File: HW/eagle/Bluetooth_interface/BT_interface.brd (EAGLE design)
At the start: 40 x 30 mm, 30 parts, among them IC3 FT232RL, IC5 UA78M05DCY

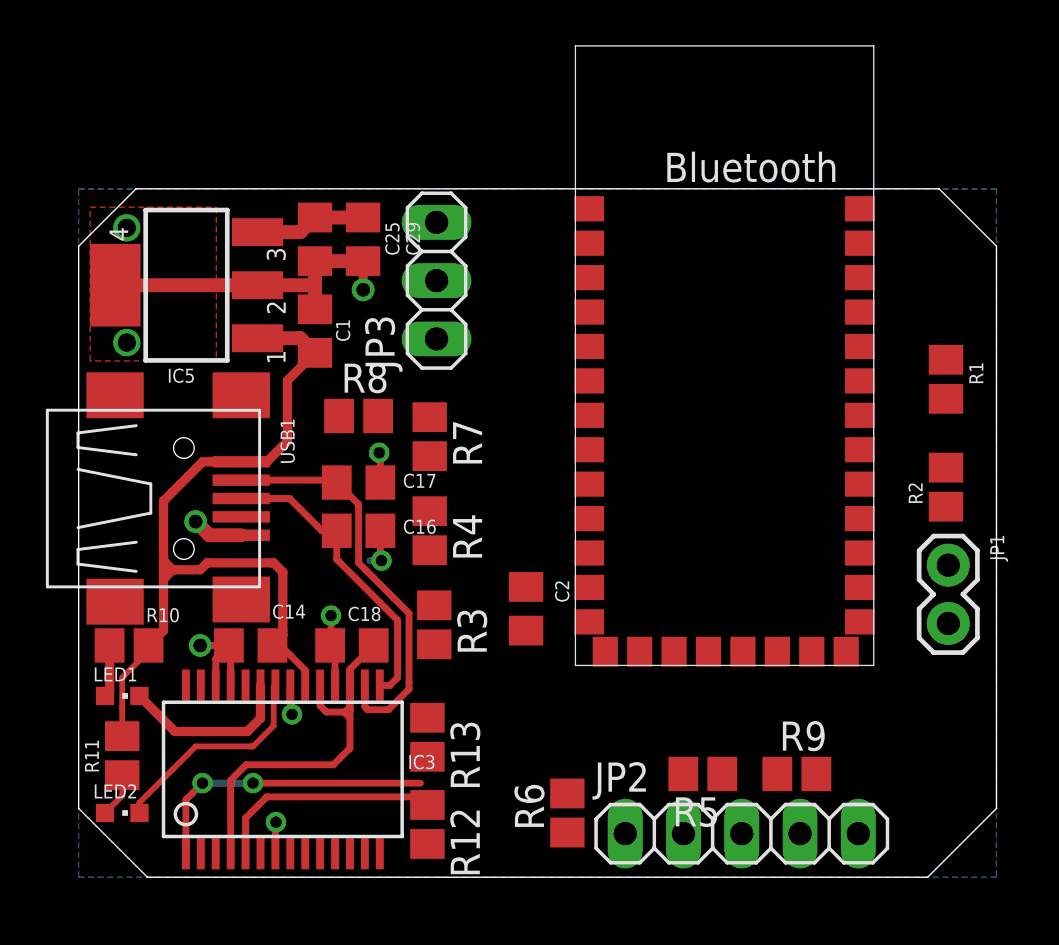
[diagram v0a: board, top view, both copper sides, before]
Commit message: labels changed, parts smashed, labels resized and rearranged
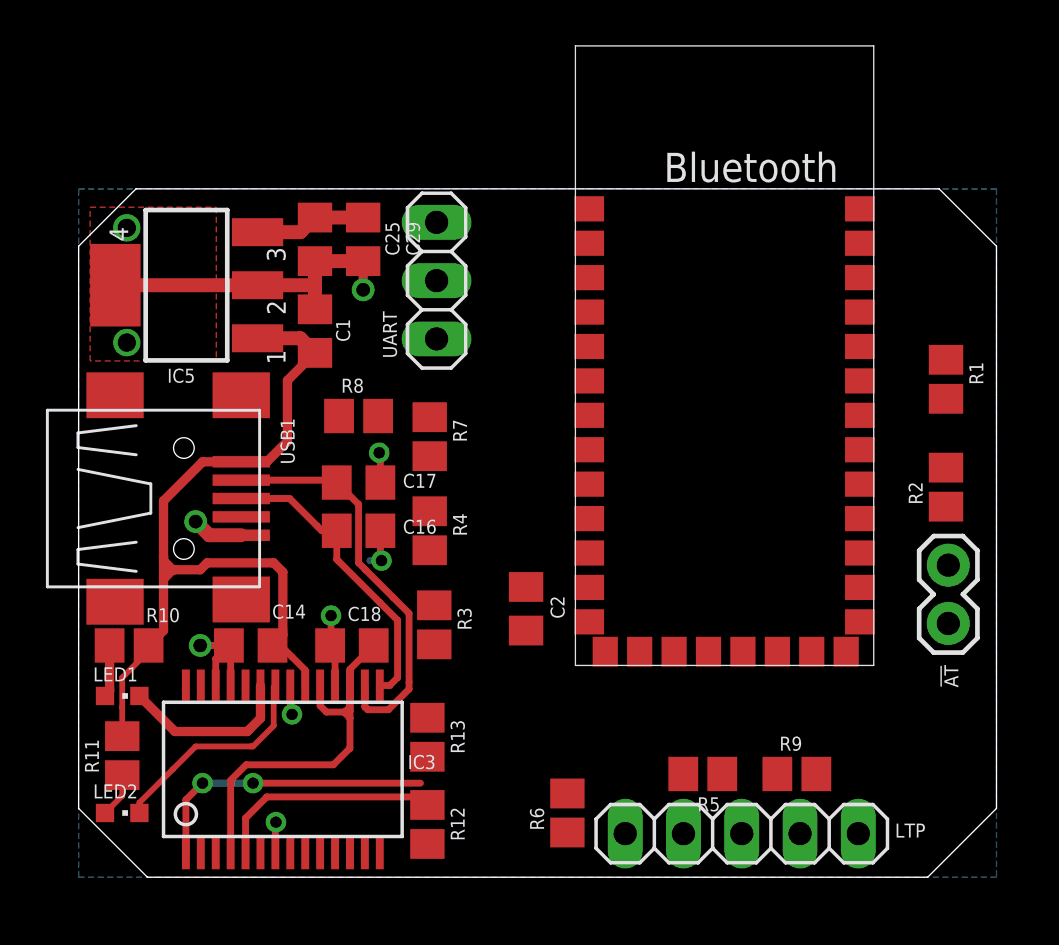
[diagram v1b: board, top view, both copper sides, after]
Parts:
- renumbered JP1 to !AT, JP2 to LTP, JP3 to UART
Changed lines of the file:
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@@
 </element>
 <element name="IC5" library="linear" package="SOT223" value="UA78M05DCY" x="4.7" y="25.8" smashed="yes" rot="R90">
-<attribute name="LM1007" value="LM1007" x="7.24" y="15.64" size="1.778" layer="27" rot="R90" display="off"/>
+<attribute name="LM1117" value="LM1117" x="7.24" y="15.64" size="1.778" layer="27" rot="R90" display="off"/>
 <attribute name="NAME" x="3.86" y="21.5508" size="0.6096" layer="25" font="vector"/>
 <attribute name="VALUE" x="6.0208" y="23.26" size="0.6096" layer="27" rot="R90"/>
@@
 </element>
 <element name="C2" library="rcl" package="C0805" value="100nF" x="19.5" y="11.7" smashed="yes" rot="R270">
-<attribute name="NAME" x="20.77" y="12.97" size="0.6096" layer="25" font="vector" rot="R270"/>
+<attribute name="NAME" x="20.57" y="12.27" size="0.6096" layer="25" font="vector" rot="R270"/>
 <attribute name="VALUE" x="16.96" y="12.97" size="1.27" layer="27" rot="R270"/>
 </element>
-<element name="JP1" library="daGloane" package="1X02" value="" x="37.9" y="13.6" smashed="yes" rot="R270">
-<attribute name="NAME" x="39.7288" y="14.9462" size="0.6096" layer="25" font="vector" ratio="10" rot="R270"/>
+<element name="!AT" library="daGloane" package="1X02" value="" x="37.9" y="13.6" smashed="yes" rot="R270">
+<attribute name="NAME" x="37.7288" y="9.2462" size="0.6096" layer="25" font="vector" ratio="10" rot="R270"/>
 <attribute name="VALUE" x="34.725" y="14.87" size="1.27" layer="27" rot="R270"/>
 </element>
@@
 <attribute name="VALUE" x="40.086" y="16.238" size="1.27" layer="27" rot="R90"/>
 </element>
-<element name="R3" library="rcl" package="R0805" value="1k6" x="15.5" y="11" rot="R270"/>
-<element name="R4" library="rcl" package="R0805" value="3k" x="15.3" y="15.1" rot="R270"/>
-<element name="R5" library="rcl" package="R0805" value="1k6" x="27.2" y="4.5" rot="R180"/>
-<element name="R6" library="rcl" package="R0805" value="3k" x="21.3" y="2.8" rot="R90"/>
-<element name="R7" library="rcl" package="R0805" value="1k6" x="15.3" y="19.2" rot="R270"/>
-<element name="R8" library="rcl" package="R0805" value="3k" x="12.2" y="20.1"/>
-<element name="R9" library="rcl" package="R0805" value="100" x="31.3" y="4.5"/>
-<element name="JP2" library="pinhead" package="1X05" value="" x="28.9" y="1.9"/>
-<element name="R12" library="rcl" package="R0805" value="4k7" x="15.2" y="2.3" rot="R270"/>
-<element name="R13" library="rcl" package="R0805" value="4k7" x="15.2" y="6.1" rot="R270"/>
-<element name="JP3" library="pinhead" package="1X03" value="" x="15.6" y="26" rot="R90"/>
+<element name="R3" library="rcl" package="R0805" value="1k6" x="15.5" y="11" smashed="yes" rot="R270">
+<attribute name="NAME" x="16.516" y="11.762" size="0.6096" layer="25" font="vector" rot="R270"/>
+<attribute name="VALUE" x="13.214" y="11.762" size="1.27" layer="27" rot="R270"/>
+</element>
+<element name="R4" library="rcl" package="R0805" value="3k" x="15.3" y="15.1" smashed="yes" rot="R270">
+<attribute name="NAME" x="16.316" y="15.862" size="0.6096" layer="25" font="vector" rot="R270"/>
+<attribute name="VALUE" x="13.014" y="15.862" size="1.27" layer="27" rot="R270"/>
+</element>
+<element name="R5" library="rcl" package="R0805" value="1k6" x="27.2" y="4.5" smashed="yes" rot="R180">
+<attribute name="NAME" x="27.962" y="3.484" size="0.6096" layer="25" font="vector" rot="R180"/>
+<attribute name="VALUE" x="27.962" y="6.786" size="1.27" layer="27" rot="R180"/>
+</element>
+<element name="R6" library="rcl" package="R0805" value="3k" x="21.3" y="2.8" smashed="yes" rot="R90">
+<attribute name="NAME" x="20.284" y="2.038" size="0.6096" layer="25" font="vector" rot="R90"/>
+<attribute name="VALUE" x="23.586" y="2.038" size="1.27" layer="27" rot="R90"/>
+</element>
+<element name="R7" library="rcl" package="R0805" value="1k6" x="15.3" y="19.2" smashed="yes" rot="R270">
+<attribute name="NAME" x="16.316" y="19.962" size="0.6096" layer="25" font="vector" rot="R270"/>
+<attribute name="VALUE" x="13.014" y="19.962" size="1.27" layer="27" rot="R270"/>
+</element>
+<element name="R8" library="rcl" package="R0805" value="3k" x="12.2" y="20.1" smashed="yes">
+<attribute name="NAME" x="11.438" y="21.116" size="0.6096" layer="25" font="vector"/>
+<attribute name="VALUE" x="11.438" y="17.814" size="1.27" layer="27"/>
+</element>
+<element name="R9" library="rcl" package="R0805" value="100" x="31.3" y="4.5" smashed="yes">
+<attribute name="NAME" x="30.538" y="5.516" size="0.6096" layer="25" font="vector"/>
+<attribute name="VALUE" x="30.538" y="2.214" size="1.27" layer="27"/>
+</element>
+<element name="LTP" library="pinhead" package="1X05" value="" x="28.9" y="1.9" smashed="yes">
+<attribute name="NAME" x="35.5738" y="1.7288" size="0.6096" layer="25" font="vector" ratio="10"/>
+<attribute name="VALUE" x="22.55" y="-1.275" size="1.27" layer="27"/>
+</element>
+<element name="R12" library="rcl" package="R0805" value="4k7" x="15.2" y="2.3" smashed="yes" rot="R270">
+<attribute name="NAME" x="16.216" y="3.062" size="0.6096" layer="25" font="vector" rot="R270"/>
+<attribute name="VALUE" x="12.914" y="3.062" size="1.27" layer="27" rot="R270"/>
+</element>
+<element name="R13" library="rcl" package="R0805" value="4k7" x="15.2" y="6.1" smashed="yes" rot="R270">
+<attribute name="NAME" x="16.216" y="6.862" size="0.6096" layer="25" font="vector" rot="R270"/>
+<attribute name="VALUE" x="12.914" y="6.862" size="1.27" layer="27" rot="R270"/>
+</element>
+<element name="UART" library="pinhead" package="1X03" value="" x="15.6" y="26" smashed="yes" rot="R90">
+<attribute name="NAME" x="13.8712" y="22.6138" size="0.6096" layer="25" font="vector" ratio="10" rot="R90"/>
+<attribute name="VALUE" x="18.775" y="22.19" size="1.27" layer="27" rot="R90"/>
+</element>
 </elements>
 <signals>
@@
 <contactref element="U$1" pad="P$13"/>
 <contactref element="C2" pad="2"/>
-<contactref element="JP1" pad="2"/>
+<contactref element="!AT" pad="2"/>
 <contactref element="R6" pad="1"/>
 <contactref element="R8" pad="1"/>
 <contactref element="R4" pad="1"/>
-<contactref element="JP2" pad="5"/>
-<contactref element="JP3" pad="2"/>
+<contactref element="LTP" pad="5"/>
+<contactref element="UART" pad="2"/>
 <via x="2.1" y="28.3" extent="1-16" drill="0.8"/>
 <via x="2.1" y="23.3" extent="1-16" drill="0.8"/>
@@
 <contactref element="R1" pad="2"/>
 <contactref element="R2" pad="1"/>
-<contactref element="JP1" pad="1"/>
+<contactref element="!AT" pad="1"/>
 <wire x1="37.8" y1="16.15" x2="37.8" y2="20.85" width="0" layer="19" extent="1-1"/>
 <wire x1="37.9" y1="13.6" x2="37.8" y2="16.15" width="0" layer="19" extent="1-1"/>
@@
 <signal name="CLK">
 <contactref element="R3" pad="2"/>
-<contactref element="JP2" pad="1"/>
+<contactref element="LTP" pad="1"/>
 <wire x1="23.82" y1="1.9" x2="15.5" y2="10.15" width="0" layer="19" extent="1-1"/>
 </signal>
 <signal name="MOSI">
 <contactref element="R5" pad="2"/>
-<contactref element="JP2" pad="2"/>
+<contactref element="LTP" pad="2"/>
 <wire x1="26.36" y1="1.9" x2="26.35" y2="4.5" width="0" layer="19" extent="1-1"/>
 </signal>
 <signal name="CSB">
 <contactref element="R7" pad="2"/>
-<contactref element="JP2" pad="3"/>
+<contactref element="LTP" pad="3"/>
 <wire x1="28.9" y1="1.9" x2="15.3" y2="18.35" width="0" layer="19" extent="1-1"/>
 </signal>
@@
 <signal name="MISO">
 <contactref element="R9" pad="2"/>
-<contactref element="JP2" pad="4"/>
+<contactref element="LTP" pad="4"/>
 <wire x1="31.44" y1="1.9" x2="32.15" y2="4.5" width="0" layer="19" extent="1-1"/>
 </signal>
@@
 <contactref element="R12" pad="1"/>
 <contactref element="U$1" pad="P$1"/>
-<contactref element="JP3" pad="3"/>
+<contactref element="UART" pad="3"/>
 <wire x1="15.6" y1="28.54" x2="22.25" y2="29.13" width="0" layer="19" extent="1-1"/>
 <wire x1="15.2" y1="3.15" x2="15.6" y2="28.54" width="0" layer="19" extent="1-1"/>
@@
 <contactref element="U$1" pad="P$2"/>
 <contactref element="R13" pad="1"/>
-<contactref element="JP3" pad="1"/>
+<contactref element="UART" pad="1"/>
 <wire x1="15.6" y1="23.46" x2="22.25" y2="27.63" width="0" layer="19" extent="1-1"/>
 <wire x1="15.2" y1="6.95" x2="15.6" y2="23.46" width="0" layer="19" extent="1-1"/>

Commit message: layout finished
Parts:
- added U$10, U$11, U$2, U$3, U$4, U$5, U$6, U$7, U$8, U$9: SPRING_HEADER, daGloane:SPRING_HEADER
- moved R4 18.7 mm to (31.0, 5.00), turned to 90 degrees
- moved R3 18.6 mm to (33.1, 5.00), turned to 90 degrees
- moved R8 18.0 mm to (22.9, 5.60), turned to 270 degrees
- moved R7 14.7 mm to (20.8, 5.60), turned to 90 degrees
- moved LTP 11.9 mm to (38.2, 9.30), turned to 270 degrees
- moved R9 8.47 mm to (35.6, 11.8), turned to 270 degrees
- moved R5 8.02 mm to (35.2, 5.00), turned to 90 degrees
- moved !AT 7.32 mm to (38.4, 20.9)
- moved UART 4.43 mm to (17.0, 21.8), turned to 270 degrees
- moved C2 3.62 mm to (17.8, 14.9), turned to 180 degrees
- moved R2 3.41 mm to (35.6, 19.6), turned to 270 degrees
- moved R1 2.96 mm to (38.4, 24.6)
- moved U$1 1.50 mm to (26.8, 23.9)
- moved R6 0.67 mm to (21.9, 2.50), turned to 0 degrees
- moved LED2 0.20 mm to (1.90, 3.00)
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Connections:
- net +3V3: now also U$4.P$1, U$5.P$1
- net CLK: now also LTP.3; no longer LTP.1
- net CSB: now also LTP.5; no longer LTP.3
- net GND: now also LTP.1, U$6.P$1; no longer LTP.5
- net MISO: now also LTP.2; no longer LTP.4
- net MOSI: now also LTP.4; no longer LTP.2
- net N$1: now also U$9.P$1
- net N$10: now also U$2.P$1
- net N$11: now also U$3.P$1
- net N$15: now also U$10.P$1
- net N$7: now also U$11.P$1
- net N$8: now also U$7.P$1
- net N$9: now also U$8.P$1
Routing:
- net +3V3: track 4.87 -> 47.7 mm
- net N$10: track 0.00 -> 36.4 mm, vias 0 -> 1
- net N$11: track 0.00 -> 27.4 mm, vias 0 -> 1
- net CSB: track 0.00 -> 26.1 mm
- net N$8: track 0.00 -> 19.2 mm
- net GND: track 30.7 -> 47.2 mm, vias 10 -> 14
- net N$15: track 0.00 -> 10.5 mm
- net CLK: track 0.00 -> 7.03 mm
- net N$6: track 0.00 -> 5.84 mm
- net N$1: track 0.00 -> 5.01 mm
- net N$7: track 0.00 -> 4.82 mm
- net N$9: track 0.00 -> 4.65 mm
- net MOSI: track 0.00 -> 3.38 mm
- net MISO: track 0.00 -> 2.97 mm
- net USART_RX: track 12.9 -> 13.7 mm

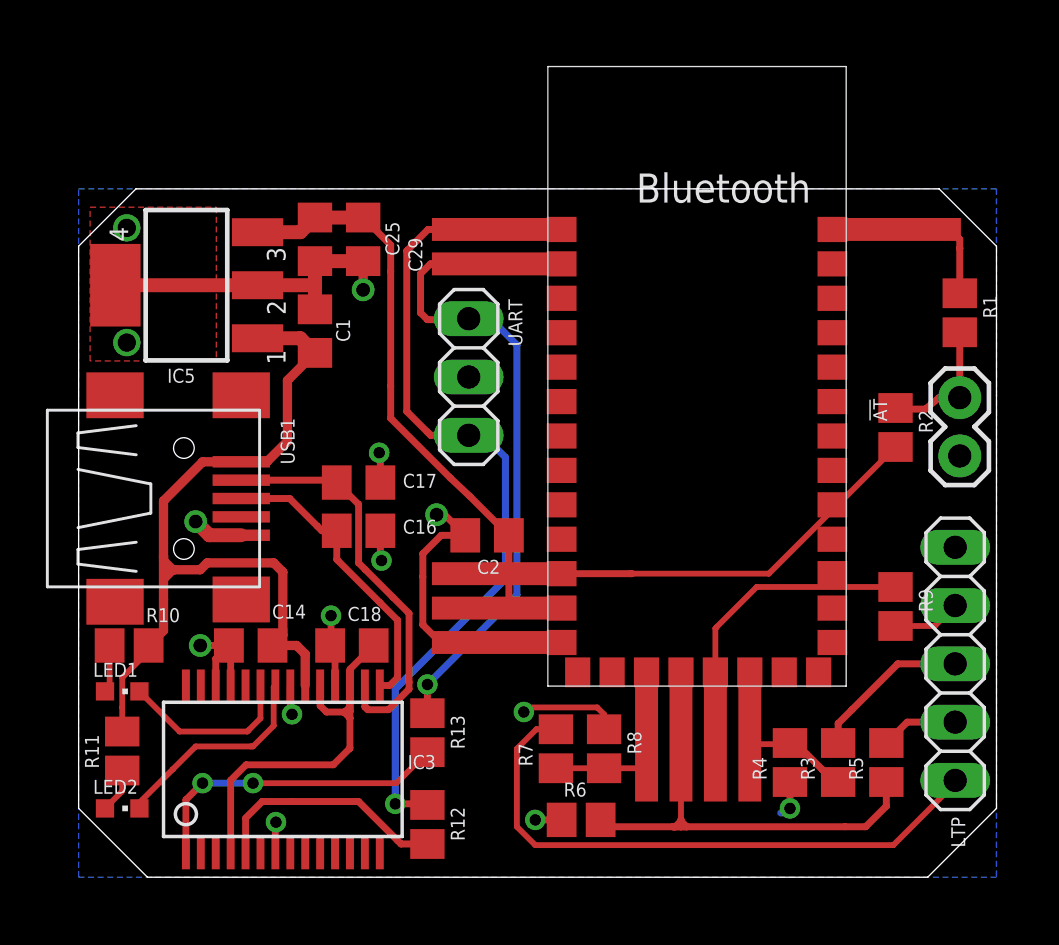
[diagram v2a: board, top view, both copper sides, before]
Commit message: added status LED
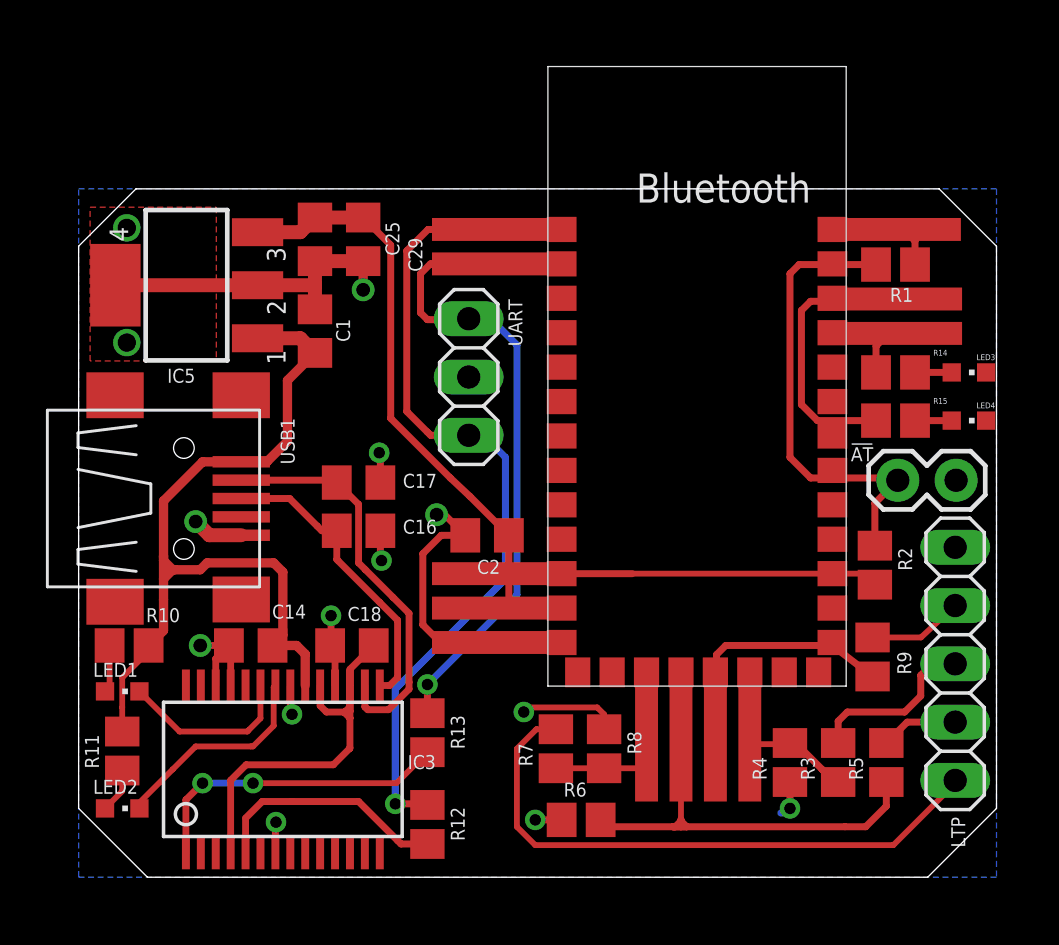
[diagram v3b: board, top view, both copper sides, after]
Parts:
- added LED3, LED4: (no value), led:CHIPLED_0603
- added R14, R15: 470R, rcl:R0805
- added U$12, U$13: SPRING_HEADER, daGloane:SPRING_HEADER
- moved R2 6.07 mm to (34.7, 13.6)
- moved !AT 4.50 mm to (35.7, 17.3), turned to 0 degrees
- moved R1 3.50 mm to (35.6, 26.7), turned to 180 degrees
- moved R9 2.42 mm to (34.6, 9.60), turned to 90 degrees
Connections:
- new net N$12: LED3.A, R14.1
- new net N$13: LED4.A, R15.1
- new net N$14: R14.2, U$1.P$31, U$13.P$1
- new net N$16: R15.2, U$1.P$32, U$12.P$1
- net GND: now also LED3.C, LED4.C
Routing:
- net N$6: track 5.84 -> 20.3 mm
- net N$16: track 0.00 -> 12.3 mm
- net +3V3: track 47.7 -> 42.4 mm
- net N$1: track 5.01 -> 1.74 mm
- net N$14: track 0.00 -> 2.63 mm
- net N$13: track 0.00 -> 1.60 mm
- net N$12: track 0.00 -> 1.60 mm
- net N$15: track 10.5 -> 9.00 mm
- net MISO: track 2.97 -> 4.15 mm
- net CLK: track 7.03 -> 7.61 mm
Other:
- outline, holes or cut-outs redrawn

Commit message: parts rearranged to leave more space for BT module
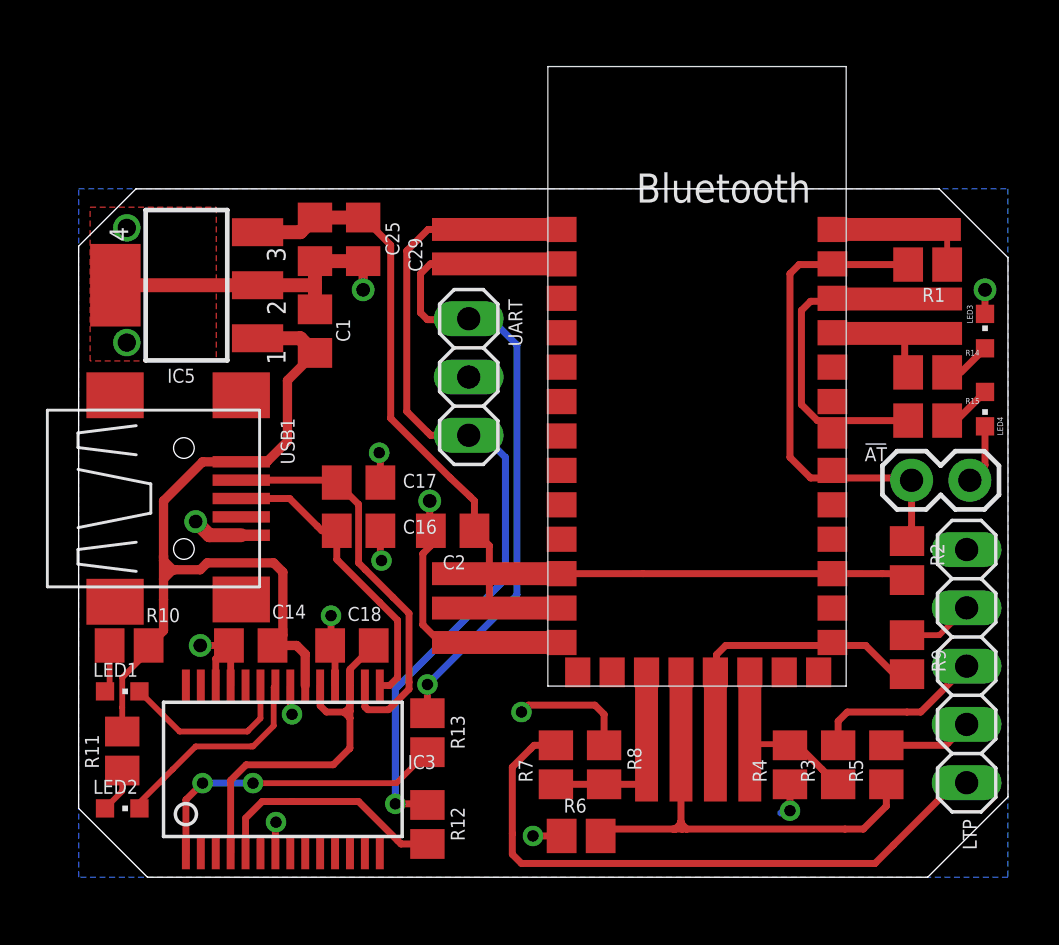
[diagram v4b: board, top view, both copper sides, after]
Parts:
- moved LED3 1.93 mm to (39.5, 23.8), turned to 0 degrees
- moved C2 1.51 mm to (16.3, 15.1)
- moved R9 1.50 mm to (36.1, 9.70)
- moved R2 1.41 mm to (36.1, 13.8)
- moved R1 1.40 mm to (37.0, 26.7)
- moved R14 1.40 mm to (37.0, 22.0)
- moved R15 1.40 mm to (37.0, 19.9)
- moved LED4 0.86 mm to (39.5, 20.4), turned to 180 degrees
- moved R6 0.70 mm to (21.9, 1.80)
- moved R7 0.70 mm to (20.8, 4.90)
- moved R8 0.70 mm to (22.9, 4.90)
- moved !AT 0.60 mm to (36.3, 17.3)
- moved LTP 0.51 mm to (38.7, 9.20)
- moved R3 0.10 mm to (33.1, 4.90)
- moved R4 0.10 mm to (31.0, 4.90)
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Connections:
- new net 3.3V: U$1.P$12
- net +3V3: no longer U$1.P$11, U$1.P$12
- net N$1: no longer U$1.P$34
- net N$10: no longer U$1.P$1
- net N$11: no longer U$1.P$2
- net N$14: no longer U$1.P$31
- net N$15: no longer U$1.P$18
- net N$16: no longer U$1.P$32
- net N$7: no longer U$1.P$16
- net N$8: no longer U$1.P$17
- net N$9: no longer U$1.P$19
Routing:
- net N$15: track 9.00 -> 13.9 mm
- net GND: track 47.2 -> 51.1 mm, vias 14 -> 15
- net +3V3: track 42.4 -> 44.6 mm
- net N$6: track 20.3 -> 22.3 mm
- net N$1: track 1.74 -> 3.43 mm
- net N$16: track 12.3 -> 13.7 mm
- net CSB: track 26.1 -> 27.5 mm
- net MISO: track 4.15 -> 3.09 mm
- net N$7: track 4.82 -> 5.52 mm
- net N$13: track 1.60 -> 2.17 mm
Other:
- board size 40 x 30 mm -> 40.5 x 30 mm
